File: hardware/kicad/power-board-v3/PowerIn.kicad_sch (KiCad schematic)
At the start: 10 parts, among them J10 Conn_01x02

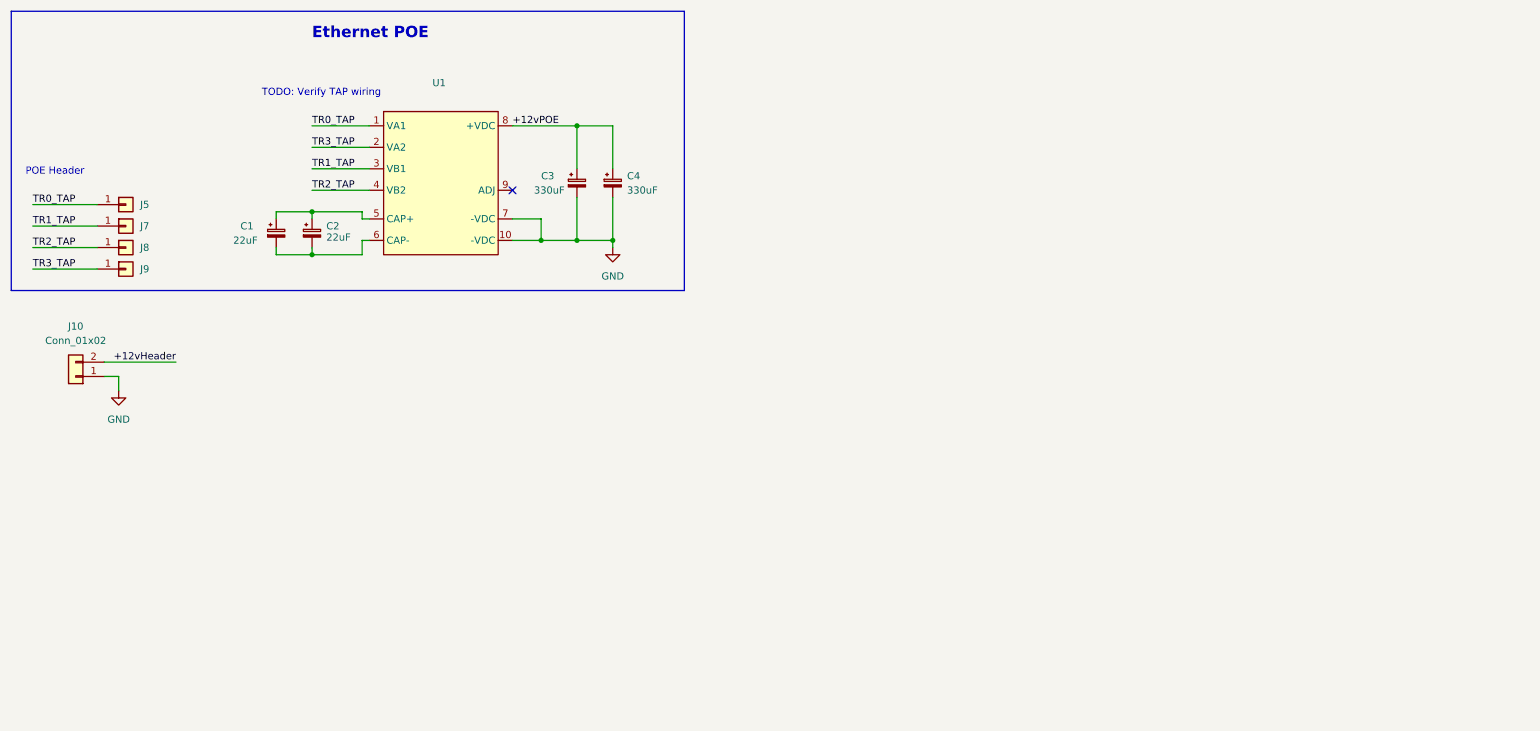
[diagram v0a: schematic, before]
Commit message: add power balance and regulator
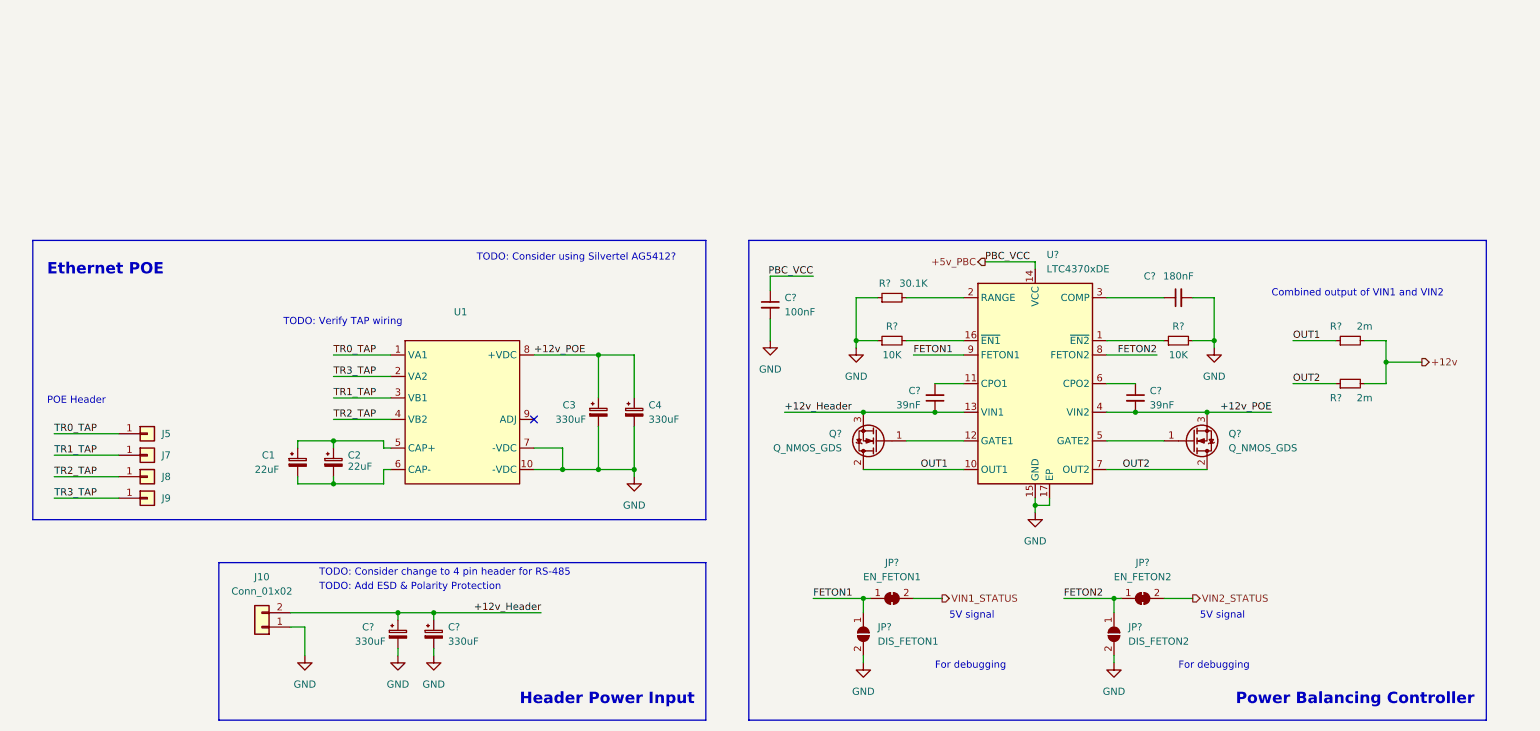
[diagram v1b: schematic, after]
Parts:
- added C?: 100nF, symbol Device:C_Small
- added C? (x2): 330uF, Capacitor_THT:CP_Radial_D8.0mm_P3.50mm, symbol Device:C_Polarized_Small
- added C? (x2): 39nF, symbol Device:C_Small
- added C?: 180nF, symbol Device:C_Small
- added JP?: EN_FETON2, symbol Jumper:SolderJumper_2_Bridged
- added JP?: EN_FETON1, symbol Jumper:SolderJumper_2_Bridged
- added JP?: DIS_FETON1, symbol Jumper:SolderJumper_2_Open
- added JP?: DIS_FETON2, symbol Jumper:SolderJumper_2_Open
- added Q? (x2): Q_NMOS_GDS, symbol Device:Q_NMOS_GDS
- added R? (x2): 10K, symbol Device:R_Small
- added R?: 30.1K, symbol Device:R_Small
- added R? (x2): 2m, symbol Device:R_Small
- added U?: LTC4370xDE, Package_DFN_QFN:DFN-16-1EP_3x4mm_P0.45mm_EP1.7x3.3mm, symbol Power_Management:LTC4370xDE
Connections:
- net GND: now also C?.2, C?.2, C?.2, C?.2, JP?.2 (B), JP?.2 (B), R?.1, R?.1, R?.2, U?.15 (GND), U?.17 (EP)
- net +12vHeader renamed +12v_Header
- net +12v_Header: now also C?.1, C?.1, C?.1, Q?.3 (S), U?.13 (VIN1)
- net +12vPOE renamed +12v_POE
- net +12v_POE: now also C?.2, Q?.3 (S), U?.4 (VIN2)
- new net: R?.1, U?.1 (~{EN2})
- new net: R?.2, U?.2 (RANGE)
- new net: R?.2, U?.16 (~{EN1})
- new net: Q?.1 (G), U?.5 (GATE2)
- new net: Q?.1 (G), U?.12 (GATE1)
- new net: C?.2, U?.11 (CPO1)
- new net: C?.1, U?.6 (CPO2)
- new net: C?.1, U?.3 (COMP)
- new net +12v: R?.2, R?.2
- new net +5v_PBC: C?.1, U?.14 (VCC)
- new net FETON1: JP?.1 (A), JP?.1 (A), U?.9 (FETON1)
- new net FETON2: JP?.1 (A), JP?.1 (A), U?.8 (FETON2)
- new net OUT1: Q?.2 (D), R?.1, U?.10 (OUT1)
- new net OUT2: Q?.2 (D), R?.1, U?.7 (OUT2)
- new net VIN1_STATUS: JP?.2 (B)
- new net VIN2_STATUS: JP?.2 (B)
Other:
- note added: "5V signal"
- note added: "Combined output of VIN1 and VIN2"
- note added: "For debugging"
- note added: "Header Power Input"
- note added: "Power Balancing Controller"
- note added: "TODO: Add ESD & Polarity Protection"
- note added: "TODO: Consider change to 4 pin header for RS-485"
- note added: "TODO: Consider using Silvertel AG5412?"
- moved on the sheet: C1, C2, C3, C4, J10, J5, J7, J8, J9, U1

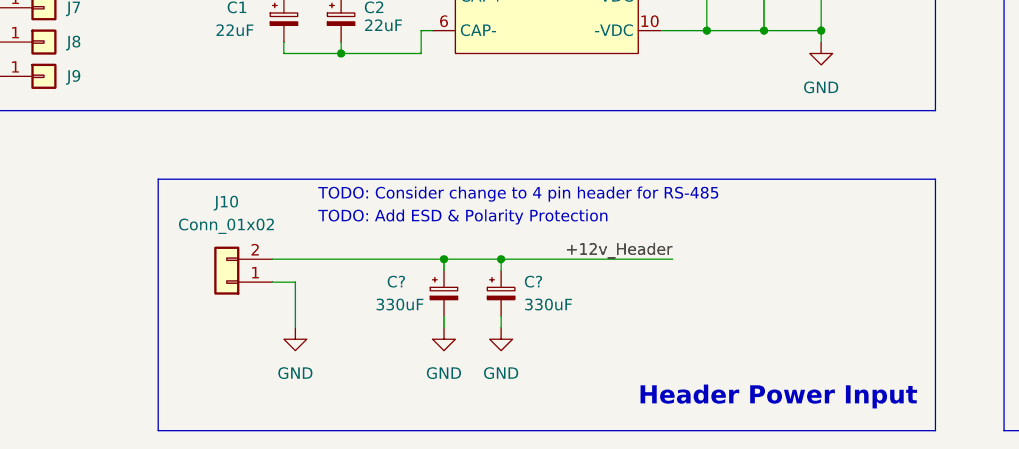
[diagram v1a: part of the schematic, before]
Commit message: add base symbol and wiring
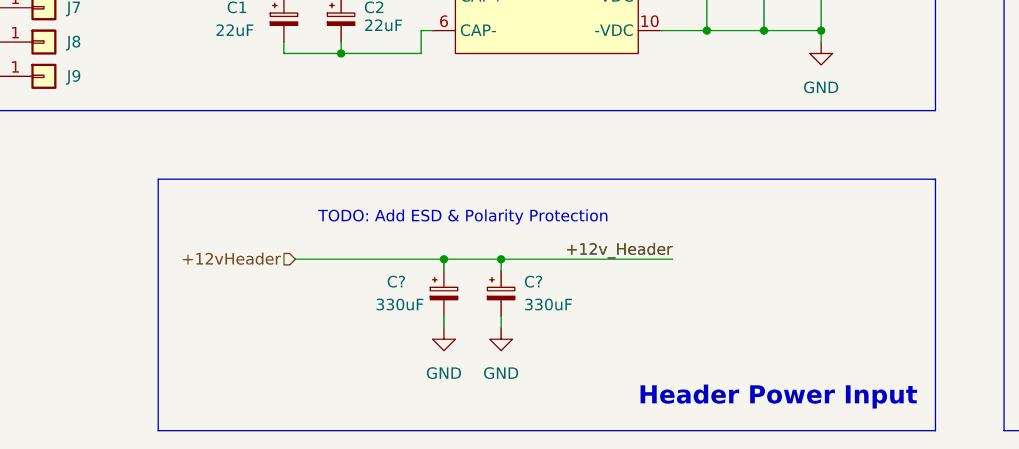
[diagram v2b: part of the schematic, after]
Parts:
- removed J10: Conn_01x02, Teapot:Molex_Micro-Fit_3.0_43650-0200_1x02_P3.00mm_Horizontal, symbol Connector_Generic:Conn_01x02
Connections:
- net +12v_Header renamed +12vHeader
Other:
- note removed: "TODO: Consider change to 4 pin header for RS-485"
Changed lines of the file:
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@@
+    (stroke (width 0) (type default) (color 0 0 0 0))
+  )
+  (wire (pts (xy 67.31 121.92) (xy 83.82 121.92))
     (stroke (width 0) (type default) (color 0 0 0 0))
   )
@@
     (stroke (width 0) (type solid) (color 0 0 0 0))
   )
-  (wire (pts (xy 64.77 121.92) (xy 83.82 121.92))
-    (stroke (width 0) (type default) (color 0 0 0 0))
-  )
   (wire (pts (xy 196.85 102.87) (xy 196.85 104.14))
     (stroke (width 0) (type default) (color 0 0 0 0))
@@
     (stroke (width 0) (type default) (color 0 0 0 0))
   )
-  (wire (pts (xy 67.31 124.46) (xy 67.31 129.54))
-    (stroke (width 0) (type default) (color 0 0 0 0))
-  )
   (wire (pts (xy 119.38 76.2) (xy 125.73 76.2))
     (stroke (width 0) (type default) (color 0 0 0 0))
@@
   )
   (wire (pts (xy 107.95 92.71) (xy 113.03 92.71))
-    (stroke (width 0) (type default) (color 0 0 0 0))
-  )
-  (wire (pts (xy 64.77 124.46) (xy 67.31 124.46))
     (stroke (width 0) (type default) (color 0 0 0 0))
   )
@@
     (effects (font (size 1.27 1.27)) (justify left bottom))
   )
-  (text "TODO: Consider change to 4 pin header for RS-485" (at 69.85 115.57 0)
-    (effects (font (size 1.27 1.27)) (justify left bottom))
-  )
   (label "TR1_TAP" (at 22.86 93.98 0)
     (effects (font (size 1.27 1.27)) (justify left bottom))
@@
     (effects (font (size 1.27 1.27)) (justify right))
   )
-  (symbol (lib_id "power:GND") (at 67.31 129.54 0) (unit 1)
-    (in_bom yes) (on_board yes) (fields_autoplaced)
-    (property "Reference" "#PWR0103" (id 0) (at 67.31 135.89 0)
-      (effects (font (size 1.27 1.27)) hide)
-    )
-    (property "Value" "GND" (id 1) (at 67.31 134.62 0))
-    (property "Footprint" "" (id 2) (at 67.31 129.54 0)
-      (effects (font (size 1.27 1.27)) hide)
-    )
-    (property "Datasheet" "" (id 3) (at 67.31 129.54 0)
-      (effects (font (size 1.27 1.27)) hide)
-    )
-    (pin "1")
+  (hierarchical_label "+12vHeader" (shape input) (at 67.31 121.92 180)
+    (effects (font (size 1.27 1.27)) (justify right))
   )
   (symbol (lib_id "power:GND") (at 210.82 130.81 0) (unit 1)
@@
       (effects (font (size 1.27 1.27)) hide)
     )
-    (pin "1")
-    (pin "2")
-  )
-  (symbol (lib_id "Connector_Generic:Conn_01x02") (at 59.69 124.46 180) (unit 1)
-    (in_bom yes) (on_board yes) (fields_autoplaced)
-    (property "Reference" "J10" (id 0) (at 59.69 115.57 0))
-    (property "Value" "Conn_01x02" (id 1) (at 59.69 118.11 0))
-    (property "Footprint" "Teapot:Molex_Micro-Fit_3.0_43650-0200_1x02_P3.00mm_Horizontal" (id 2) (at 59.69 124.46 0)
-      (effects (font (size 1.27 1.27)) hide)
-    )
-    (property "Datasheet" "~" (id 3) (at 59.69 124.46 0)
-      (effects (font (size 1.27 1.27)) hide)
-    )

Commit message: initial controller design
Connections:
- net +12vHeader renamed +12v_Header
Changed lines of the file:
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@@
     (effects (font (size 1.27 1.27)) (justify right))
   )
-  (hierarchical_label "+12vHeader" (shape input) (at 67.31 121.92 180)
+  (hierarchical_label "+12v_Header" (shape input) (at 67.31 121.92 180)
     (effects (font (size 1.27 1.27)) (justify right))
   )
